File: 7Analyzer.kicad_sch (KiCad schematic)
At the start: 30 parts, among them J1 PINHD_1x1_Male, J10 PINHD_1x3_Male, J11 PINHD_1x3_Male, J2 PINHD_1x1_Male, J3 PINHD_1x3_Male, J4 PINHD_1x3_Male, J5 PINHD_1x3_Male, J6 PINHD_1x3_Male, J7 PINHD_1x3_Male, J8 PINHD_1x3_Male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

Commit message: laengere Version
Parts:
- added J12: PINHD_1x1_Male, MountingHole:MountingHole_3.5mm_Pad, symbol PCM_SL_Pin_Headers:PINHD_1x1_Male
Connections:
- net GND: now also J12.1
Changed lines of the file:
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@@
+	)
+	(symbol
+		(lib_id "power:GND")
+		(at 53.34 176.53 0)
+		(unit 1)
+		(exclude_from_sim no)
+		(in_bom yes)
+		(on_board yes)
+		(dnp no)
+		(fields_autoplaced yes)
+		(property "Reference" "#PWR013"
+			(at 53.34 182.88 0)
+			(effects
+				(font
+					(size 1.27 1.27)
+				)
+				(hide yes)
+			)
+		)
+		(property "Value" "GND"
+			(at 53.34 181.61 0)
+			(effects
+				(font
+					(size 1.27 1.27)
+				)
+			)
+		)
+		(property "Footprint" ""
+			(at 53.34 176.53 0)
+			(effects
+				(font
+					(size 1.27 1.27)
+				)
+				(hide yes)
+			)
+		)
+		(property "Datasheet" ""
+			(at 53.34 176.53 0)
+			(effects
+				(font
+					(size 1.27 1.27)
+				)
+				(hide yes)
+			)
+		)
+		(property "Description" "Power symbol creates a global label with name \"GND\" , ground"
+			(at 53.34 176.53 0)
+			(effects
+				(font
+					(size 1.27 1.27)
+				)
+				(hide yes)
+			)
+		)
+		(pin "1"
+		)
+		(instances
+			(project "7Analyzer"
+				(path "/dceeb1a9-ad1e-485a-bb61-44ce6645b5a9"
+					(reference "#PWR013")
+					(unit 1)
+				)
+			)
+		)
 	)
 	(symbol
@@
 					(unit 1)
 				)
+			)
+		)
+	)
+	(symbol
+		(lib_id "PCM_SL_Pin_Headers:PINHD_1x1_Male")
+		(at 57.15 176.53 0)
+		(unit 1)
+		(exclude_from_sim no)
+		(in_bom yes)
+		(on_board yes)
+		(dnp no)
+		(fields_autoplaced yes)
+		(property "Reference" "J12"
+			(at 59.69 175.2599 0)
+			(effects
+				(font
+					(size 1.27 1.27)
+				)
+				(justify left)
+			)
+		)
+		(property "Value" "PINHD_1x1_Male"
+			(at 59.69 177.7999 0)
+			(effects
+				(font
+					(size 1.27 1.27)
+				)
+				(justify left)
+			)
+		)
+		(property "Footprint" "MountingHole:MountingHole_3.5mm_Pad"
+			(at 58.42 179.07 0)
+			(effects
+				(font
+					(size 1.27 1.27)
+				)
+				(hide yes)
+			)
+		)
+		(property "Datasheet" ""
+			(at 57.15 170.18 0)
+			(effects
+				(font
+					(size 1.27 1.27)
+				)
+				(hide yes)
+			)
+		)
+		(property "Description" "Pin Header male with pin space 2.54mm. Pin Count -1"
+			(at 57.15 176.53 0)
+			(effects
+				(font
+					(size 1.27 1.27)
+				)
+				(hide yes)
+			)
+		)
+		(pin "1"
+		)
+		(instances
+			(project "7Analyzer"
+				(path "/dceeb1a9-ad1e-485a-bb61-44ce6645b5a9"
+					(reference "J12")
+					(unit 1)
+				)

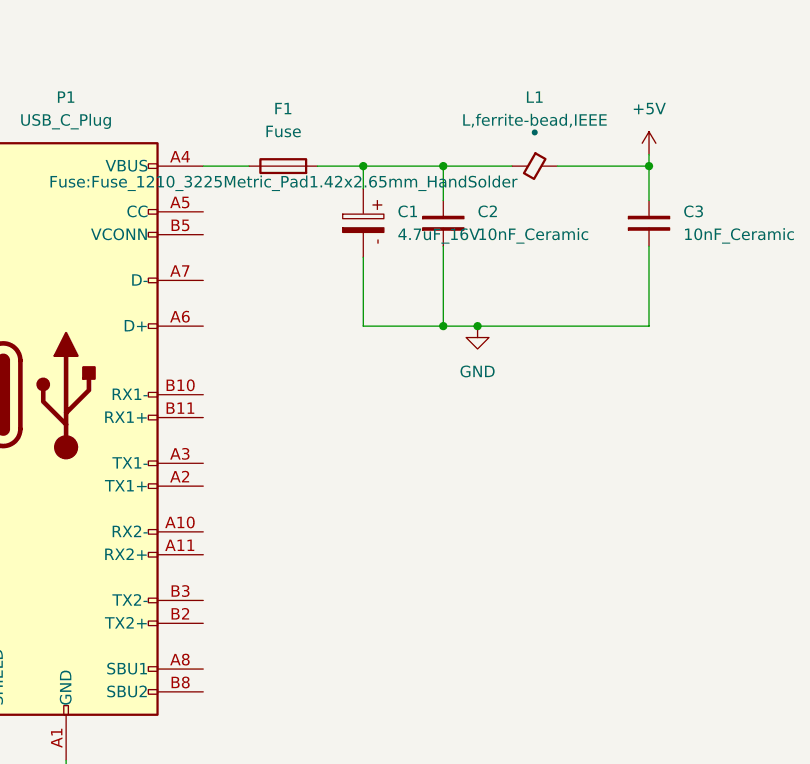
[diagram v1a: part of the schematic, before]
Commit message: add micro usb to connect esp32
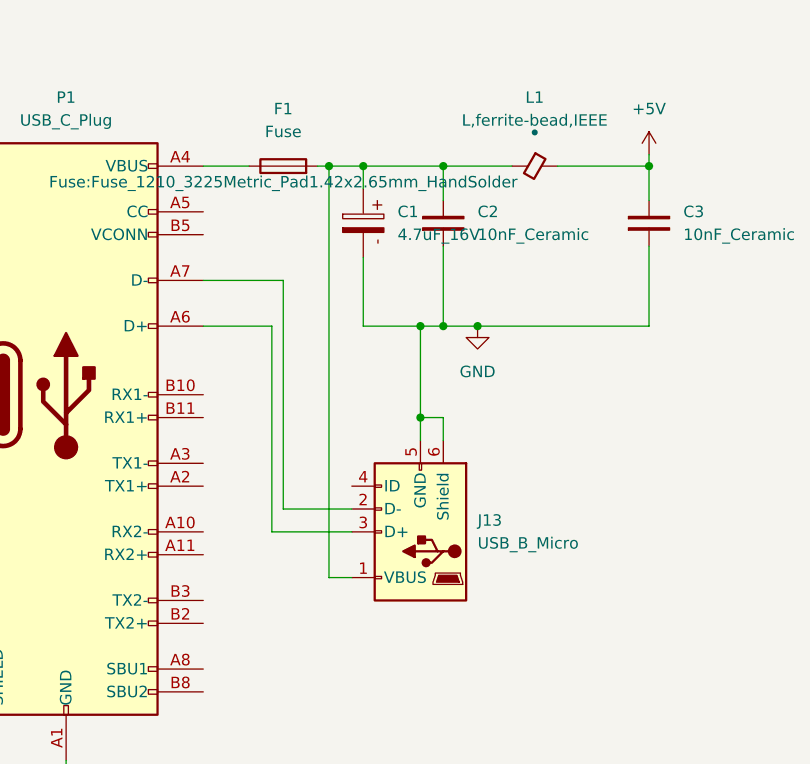
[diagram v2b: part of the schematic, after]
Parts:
- added J13: USB_B_Micro, Connector_USB:USB_Micro-B_Amphenol_10118193-0002LF_Horizontal, symbol Connector:USB_B_Micro
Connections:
- net GND: now also J13.5 (GND), J13.6 (Shield)
- net at C1.1, C2.2, F1.2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: now also J13.1 (VBUS)
- net at P1.A6 (D+): now also J13.3 (D+)
- net at P1.A7 (D-): now also J13.2 (D-)
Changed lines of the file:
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@@
 	)
 	(junction
+		(at 66.04 48.26)
+		(diameter 0)
+		(color 0 0 0 0)
+	)
+	(junction
 		(at 142.24 101.6)
 		(diameter 0)
@@
 	)
 	(junction
+		(at 66.04 38.1)
+		(diameter 0)
+		(color 0 0 0 0)
+	)
+	(junction
 		(at 91.44 20.32)
 		(diameter 0)
@@
 	)
 	(junction
+		(at 55.88 20.32)
+		(diameter 0)
+		(color 0 0 0 0)
+	)
+	(junction
 		(at 142.24 67.31)
 		(diameter 0)
@@
 	(wire
 		(pts
-			(xy 59.69 38.1) (xy 68.58 38.1)
+			(xy 59.69 38.1) (xy 66.04 38.1)
+		)
+		(stroke
+			(width 0)
+			(type default)
+		)
+	)
+	(wire
+		(pts
+			(xy 68.58 48.26) (xy 66.04 48.26)
 		)
 		(stroke
@@
 	(wire
 		(pts
+			(xy 50.8 33.02) (xy 50.8 58.42)
+		)
+		(stroke
+			(width 0)
+			(type default)
+		)
+	)
+	(wire
+		(pts
 			(xy 142.24 44.45) (xy 142.24 33.02)
 		)
@@
 		)
 	)
+	(wire
+		(pts
+			(xy 41.91 33.02) (xy 50.8 33.02)
+		)
+		(stroke
+			(width 0)
+			(type default)
+		)
+	)
 	(bus
 		(pts
@@
 	(wire
 		(pts
+			(xy 55.88 20.32) (xy 55.88 66.04)
+		)
+		(stroke
+			(width 0)
+			(type default)
+		)
+	)
+	(wire
+		(pts
 			(xy 212.09 26.67) (xy 212.09 39.37)
 		)
@@
 	(wire
 		(pts
+			(xy 66.04 38.1) (xy 66.04 48.26)
+		)
+		(stroke
+			(width 0)
+			(type default)
+		)
+	)
+	(wire
+		(pts
 			(xy 142.24 132.08) (xy 142.24 121.92)
 		)
@@
 		)
 	)
+	(wire
+		(pts
+			(xy 49.53 38.1) (xy 49.53 60.96)
+		)
+		(stroke
+			(width 0)
+			(type default)
+		)
+	)
 	(bus
 		(pts
@@
 		)
 	)
+	(wire
+		(pts
+			(xy 55.88 66.04) (xy 58.42 66.04)
+		)
+		(stroke
+			(width 0)
+			(type default)
+		)
+	)
 	(bus
 		(pts
@@
 	(wire
 		(pts
+			(xy 68.58 50.8) (xy 68.58 48.26)
+		)
+		(stroke
+			(width 0)
+			(type default)
+		)
+	)
+	(wire
+		(pts
 			(xy 134.62 38.1) (xy 138.43 38.1)
 		)
@@
 		)
 	)
+	(wire
+		(pts
+			(xy 66.04 48.26) (xy 66.04 50.8)
+		)
+		(stroke
+			(width 0)
+			(type default)
+		)
+	)
 	(bus
 		(pts
@@
 	(wire
 		(pts
+			(xy 55.88 20.32) (xy 59.69 20.32)
+		)
+		(stroke
+			(width 0)
+			(type default)
+		)
+	)
+	(wire
+		(pts
 			(xy 161.29 52.07) (xy 176.53 52.07)
 		)
@@
 	(wire
 		(pts
-			(xy 54.61 20.32) (xy 59.69 20.32)
+			(xy 50.8 58.42) (xy 58.42 58.42)
+		)
+		(stroke
+			(width 0)
+			(type default)
+		)
+	)
+	(wire
+		(pts
+			(xy 41.91 38.1) (xy 49.53 38.1)
+		)
+		(stroke
+			(width 0)
+			(type default)
+		)
+	)
+	(wire
+		(pts
+			(xy 49.53 60.96) (xy 58.42 60.96)
+		)
+		(stroke
+			(width 0)
+			(type default)
+		)
+	)
+	(wire
+		(pts
+			(xy 54.61 20.32) (xy 55.88 20.32)
 		)
 		(stroke
@@
 	(wire
 		(pts
+			(xy 66.04 38.1) (xy 68.58 38.1)
+		)
+		(stroke
+			(width 0)
+			(type default)
+		)
+	)
+	(wire
+		(pts
 			(xy 161.29 64.77) (xy 176.53 64.77)
 		)
@@
 					(unit 1)
 				)
+			)
+		)
+	)
+	(symbol
+		(lib_id "Connector:USB_B_Micro")
+		(at 66.04 60.96 180)
+		(unit 1)
+		(exclude_from_sim no)
+		(in_bom yes)
+		(on_board yes)
+		(dnp no)
+		(fields_autoplaced yes)
+		(property "Reference" "J13"
+			(at 72.39 59.6899 0)
+			(effects
+				(font
+					(size 1.27 1.27)
+				)
+				(justify right)
+			)
+		)
+		(property "Value" "USB_B_Micro"
+			(at 72.39 62.2299 0)
+			(effects
+				(font
+					(size 1.27 1.27)
+				)
+				(justify right)
+			)
+		)
+		(property "Footprint" "Connector_USB:USB_Micro-B_Amphenol_10118193-0002LF_Horizontal"
+			(at 62.23 59.69 0)
+			(effects
+				(font
+					(size 1.27 1.27)
+				)
+				(hide yes)
+			)
+		)
+		(property "Datasheet" "~"
+			(at 62.23 59.69 0)
+			(effects
+				(font
+					(size 1.27 1.27)
+				)
+				(hide yes)
+			)
+		)
+		(property "Description" "USB Micro Type B connector"
+			(at 66.04 60.96 0)
+			(effects
+				(font
+					(size 1.27 1.27)
+				)
+				(hide yes)
+			)
+		)
+		(pin "1"
+		)
+		(pin "5"
+		)
+		(pin "4"
+		)
+		(pin "2"
+		)
+		(pin "6"
+		)
+		(pin "3"
+		)
+		(instances
+			(project ""
+				(path "/dceeb1a9-ad1e-485a-bb61-44ce6645b5a9"
+					(reference "J13")
+					(unit 1)
+				)

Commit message: ich hab keine Ahnung
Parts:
- added R1, R2: 5.1k, Resistor_SMD:R_0805_2012Metric_Pad1.20x1.40mm_HandSolder, symbol PCM_SL_Resistors:5.6k
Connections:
- net GND: now also R1.2, R2.2
- net at P1.A5 (CC): now also R1.1
- net at P1.B5 (VCONN): now also R2.1

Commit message: create gerber files for v2
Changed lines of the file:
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@@
 		(dnp no)
 		(property "Reference" "R1"
-			(at 46.99 23.876 0)
+			(at 50.8 24.13 0)
 			(effects
 				(font
@@
 		)
 		(property "Value" "5.1k"
-			(at 48.514 27.178 0)
+			(at 51.308 26.67 0)
 			(effects
 				(font
@@
 		(on_board yes)
 		(dnp no)
-		(fields_autoplaced yes)
 		(property "Reference" "C11"
-			(at 208.28 29.2099 90)
+			(at 190.754 30.734 90)
 			(effects
 				(font
@@
 		)
 		(property "Value" "10nF_Ceramic"
-			(at 208.28 31.7499 90)
+			(at 190.5 32.512 90)
 			(effects
 				(font
@@
 		(on_board yes)
 		(dnp no)
-		(fields_autoplaced yes)
 		(property "Reference" "C2"
-			(at 72.39 25.3999 90)
+			(at 68.834 28.702 90)
 			(effects
 				(font
@@
 		)
 		(property "Value" "10nF_Ceramic"
-			(at 72.39 27.9399 90)
+			(at 69.088 30.48 90)
 			(effects
 				(font
@@
 		(on_board yes)
 		(dnp no)
-		(fields_autoplaced yes)
 		(property "Reference" "#PWR05"
 			(at 209.55 30.48 0)
@@
 		)
 		(property "Value" "+5V"
-			(at 209.55 21.59 0)
+			(at 207.01 24.384 0)
 			(effects
 				(font
@@
 		(dnp no)
 		(property "Reference" "R2"
-			(at 46.736 28.956 0)
+			(at 50.546 29.21 0)
 			(effects
 				(font
@@
 		)
 		(property "Value" "5.1k"
-			(at 47.244 32.512 0)
+			(at 51.308 31.75 0)
 			(effects
 				(font
@@
 		(on_board yes)
 		(dnp no)
-		(fields_autoplaced yes)
 		(property "Reference" "#PWR09"
 			(at 212.09 30.48 0)
@@
 		)
 		(property "Value" "+3.3V"
-			(at 212.09 21.59 0)
+			(at 215.392 24.13 0)
 			(effects
 				(font
@@
 		(on_board yes)
 		(dnp no)
-		(fields_autoplaced yes)
 		(property "Reference" "L1"
-			(at 78.74 12.7 90)
+			(at 71.628 15.494 90)
 			(effects
 				(font
@@
 		)
 		(property "Value" "L,ferrite-bead,IEEE"
-			(at 78.74 15.24 90)
+			(at 79.756 17.78 90)
 			(effects
 				(font
@@
 		(on_board yes)
 		(dnp no)
-		(fields_autoplaced yes)
 		(property "Reference" "C1"
-			(at 63.5 25.3999 90)
+			(at 56.642 28.702 90)
 			(effects
 				(font
@@
 		)
 		(property "Value" "4.7uF_16V"
-			(at 63.5 27.9399 90)
+			(at 56.642 30.48 90)
 			(effects
 				(font
